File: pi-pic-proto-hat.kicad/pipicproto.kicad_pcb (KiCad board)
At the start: 2 copper layers, 65 x 56 mm, 26 parts, among them J1 RUN/~PGM~, J10 Conn_01x13_Male, J2 Conn_SW1, J22 Conn_01x13_Male, J6 Barrel_Jack_Switch, J7 Conn_01x24_Male, J8 Conn_01x06_Male, J9 Conn_01x02_Male, P1 Conn_02x20_Odd_Even, Q1 IRF4905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

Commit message: moved button to right of power-jack
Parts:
- added ?: , , F.Cu at (244.4, 129.5)
- added ?: , , F.Cu at (244.7, 129.1)
- moved SW1 18.4 mm to (258.5, 129.9), turned to 180 degrees
- moved J2 6.39 mm to (247.2, 130.5), turned to 180 degrees
- moved J9 2.09 mm to (247.3, 124.0)
- moved U1 2.09 mm to (257.2, 124.1)
- moved R5 2.09 mm to (258.9, 117.4)
- moved C1 2.09 mm to (251.7, 126.9)
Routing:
- net Net-(J2-Pad2): track 28.0 -> 32.2 mm, vias 0 -> 1
- net +5VP: track 20.9 -> 25.0 mm
- net /MCLR: track 9.64 -> 6.06 mm
- net GND: track 36.1 -> 39.5 mm
- net /DAT: track 8.27 -> 10.8 mm
- net /CLK: track 19.3 -> 21.1 mm
- net /GPIO16: track 34.9 -> 33.4 mm
- net Net-(R2-Pad2): track 28.3 -> 29.2 mm
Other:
- board text added: "(SW1)"

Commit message: V2.14: removed dead button from power connector
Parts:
- removed ? (x2): , 
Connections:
- J22 pad 7: Net-(J22-Pad7) -> +3V3

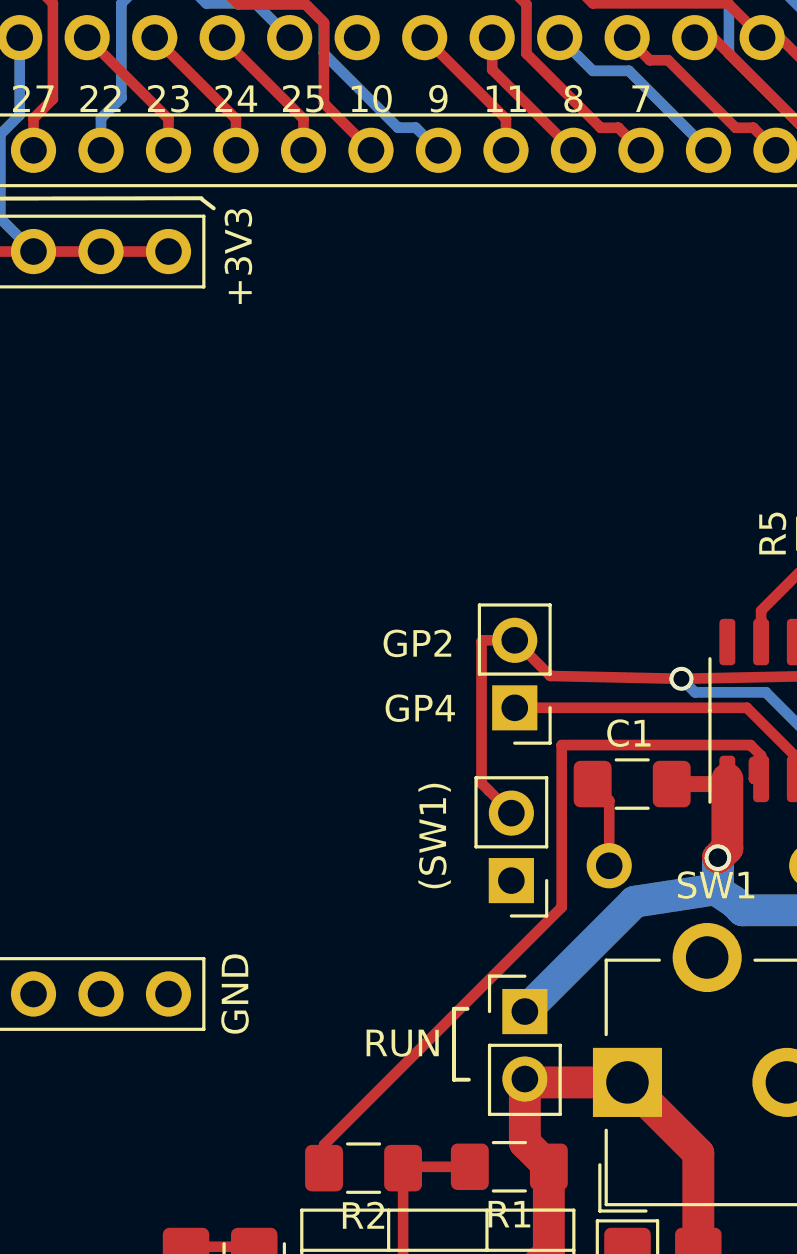
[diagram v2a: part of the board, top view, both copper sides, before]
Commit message: V2.15: added connector for +5P (5V permanently on)
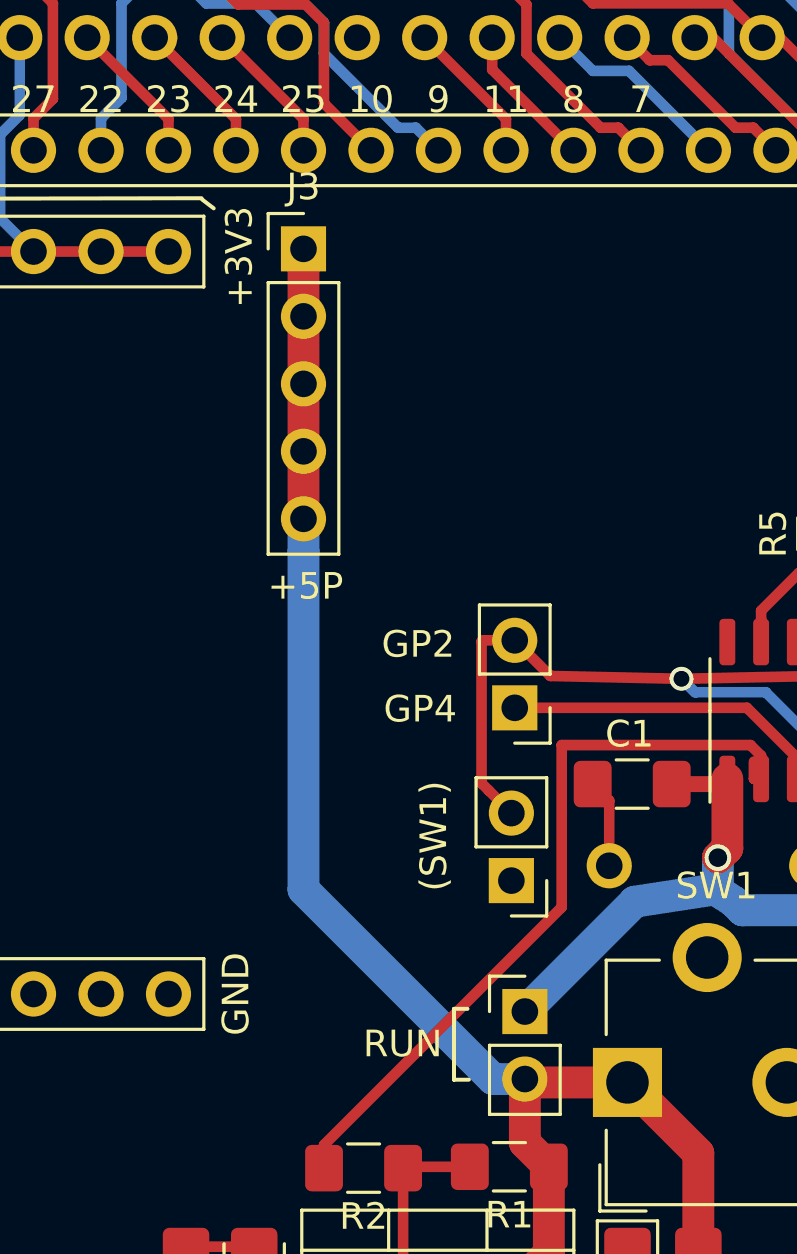
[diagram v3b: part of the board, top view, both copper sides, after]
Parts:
- added J3: Conn_01x05_Male, Connector_PinHeader_2.54mm:PinHeader_1x05_P2.54mm_Vertical, F.Cu at (239.4, 106.7)
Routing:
- net +5P: track 20.5 -> 55.9 mm
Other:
- board text added: "+5P"
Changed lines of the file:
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@@
   (general
     (thickness 1.6)
-    (drawings 68)
-    (tracks 249)
+    (drawings 69)
+    (tracks 257)
     (zones 0)
-    (modules 26)
+    (modules 27)
     (nets 45)
   )
@@
     (add_net +5VP)
   )
+  (module Connector_PinHeader_2.54mm:PinHeader_1x05_P2.54mm_Vertical (layer F.Cu)
+    (at 239.37 106.7184)
+    (descr "Through hole straight pin header, 1x05, 2.54mm pitch, single row")
+    (tags "Through hole pin header THT 1x05 2.54mm single row")
+    (fp_text reference J3 (at 0 -2.33) (layer F.SilkS)
+      (effects (font (size 1 1) (thickness 0.15)))
+    )
+    (fp_text value Conn_01x05_Male (at 0 12.49) (layer F.Fab)
+      (effects (font (size 1 1) (thickness 0.15)))
+    )
+    (fp_text user %R (at 0 5.08 90) (layer F.Fab)
+      (effects (font (size 1 1) (thickness 0.15)))
+    )
+    (fp_line (start 1.8 -1.8) (end -1.8 -1.8) (layer F.CrtYd) (width 0.05))
+    (fp_line (start 1.8 11.95) (end 1.8 -1.8) (layer F.CrtYd) (width 0.05))
+    (fp_line (start -1.8 11.95) (end 1.8 11.95) (layer F.CrtYd) (width 0.05))
+    (fp_line (start -1.8 -1.8) (end -1.8 11.95) (layer F.CrtYd) (width 0.05))
+    (fp_line (start -1.33 -1.33) (end 0 -1.33) (layer F.SilkS) (width 0.12))
+    (fp_line (start -1.33 0) (end -1.33 -1.33) (layer F.SilkS) (width 0.12))
+    (fp_line (start -1.33 1.27) (end 1.33 1.27) (layer F.SilkS) (width 0.12))
+    (fp_line (start 1.33 1.27) (end 1.33 11.49) (layer F.SilkS) (width 0.12))
+    (fp_line (start -1.33 1.27) (end -1.33 11.49) (layer F.SilkS) (width 0.12))
+    (fp_line (start -1.33 11.49) (end 1.33 11.49) (layer F.SilkS) (width 0.12))
+    (fp_line (start -1.27 -0.635) (end -0.635 -1.27) (layer F.Fab) (width 0.1))
+    (fp_line (start -1.27 11.43) (end -1.27 -0.635) (layer F.Fab) (width 0.1))
+    (fp_line (start 1.27 11.43) (end -1.27 11.43) (layer F.Fab) (width 0.1))
+    (fp_line (start 1.27 -1.27) (end 1.27 11.43) (layer F.Fab) (width 0.1))
+    (fp_line (start -0.635 -1.27) (end 1.27 -1.27) (layer F.Fab) (width 0.1))
+    (pad 5 thru_hole oval (at 0 10.16) (size 1.7 1.7) (drill 1) (layers *.Cu *.Mask)
+      (net 41 +5P))
+    (pad 4 thru_hole oval (at 0 7.62) (size 1.7 1.7) (drill 1) (layers *.Cu *.Mask)
+      (net 41 +5P))
+    (pad 3 thru_hole oval (at 0 5.08) (size 1.7 1.7) (drill 1) (layers *.Cu *.Mask)
+      (net 41 +5P))
+    (pad 2 thru_hole oval (at 0 2.54) (size 1.7 1.7) (drill 1) (layers *.Cu *.Mask)
+      (net 41 +5P))
+    (pad 1 thru_hole rect (at 0 0) (size 1.7 1.7) (drill 1) (layers *.Cu *.Mask)
+      (net 41 +5P))
+    (model ${KISYS3DMOD}/Connector_PinHeader_2.54mm.3dshapes/PinHeader_1x05_P2.54mm_Vertical.wrl
+      (at (xyz 0 0 0))
+      (scale (xyz 1 1 1))
+      (rotate (xyz 0 0 0))
+    )
+  )
   (module user:SW_PUSH_SLIM_1x4 (layer F.Cu)
     (at 258.4962 129.934 180)
@@
       (rotate (xyz 0 0 0))
     )
+  )
+  (gr_text +5P (at 239.4462 119.4184) (layer F.SilkS)
+    (effects (font (size 1 1) (thickness 0.15)))
   )
   (gr_text "(SW1)" (at 244.2722 128.8164 90) (layer F.SilkS)
@@
   (segment (start 247.7012 140.3591) (end 248.6045 141.2624) (width 1.2) (layer F.Cu) (net 41) (status 20))
   (segment (start 247.7012 137.9604) (end 247.7012 140.3591) (width 1.2) (layer F.Cu) (net 41) (status 10))
+  (segment (start 239.37 118.080481) (end 239.37 116.8784) (width 1.2) (layer B.Cu) (net 41))
+  (segment (start 239.37 130.831281) (end 239.37 118.080481) (width 1.2) (layer B.Cu) (net 41))
+  (segment (start 246.499119 137.9604) (end 239.37 130.831281) (width 1.2) (layer B.Cu) (net 41))
+  (segment (start 247.7012 137.9604) (end 246.499119 137.9604) (width 1.2) (layer B.Cu) (net 41))
+  (segment (start 239.37 116.8784) (end 239.37 114.3384) (width 1.2) (layer F.Cu) (net 41))
+  (segment (start 239.37 111.7984) (end 239.37 109.2584) (width 1.2) (layer F.Cu) (net 41))
+  (segment (start 239.37 109.2584) (end 239.37 106.7184) (width 1.2) (layer F.Cu) (net 41))
+  (segment (start 239.37 114.3384) (end 239.37 111.7984) (width 1.2) (layer F.Cu) (net 41))
   (segment (start 237.5158 144.2707) (end 234.9504 144.2707) (width 0.4) (layer F.Cu) (net 42) (status 30))
   (segment (start 254.229 147.2457) (end 251.562 147.2457) (width 0.4) (layer F.Cu) (net 43) (status 30))

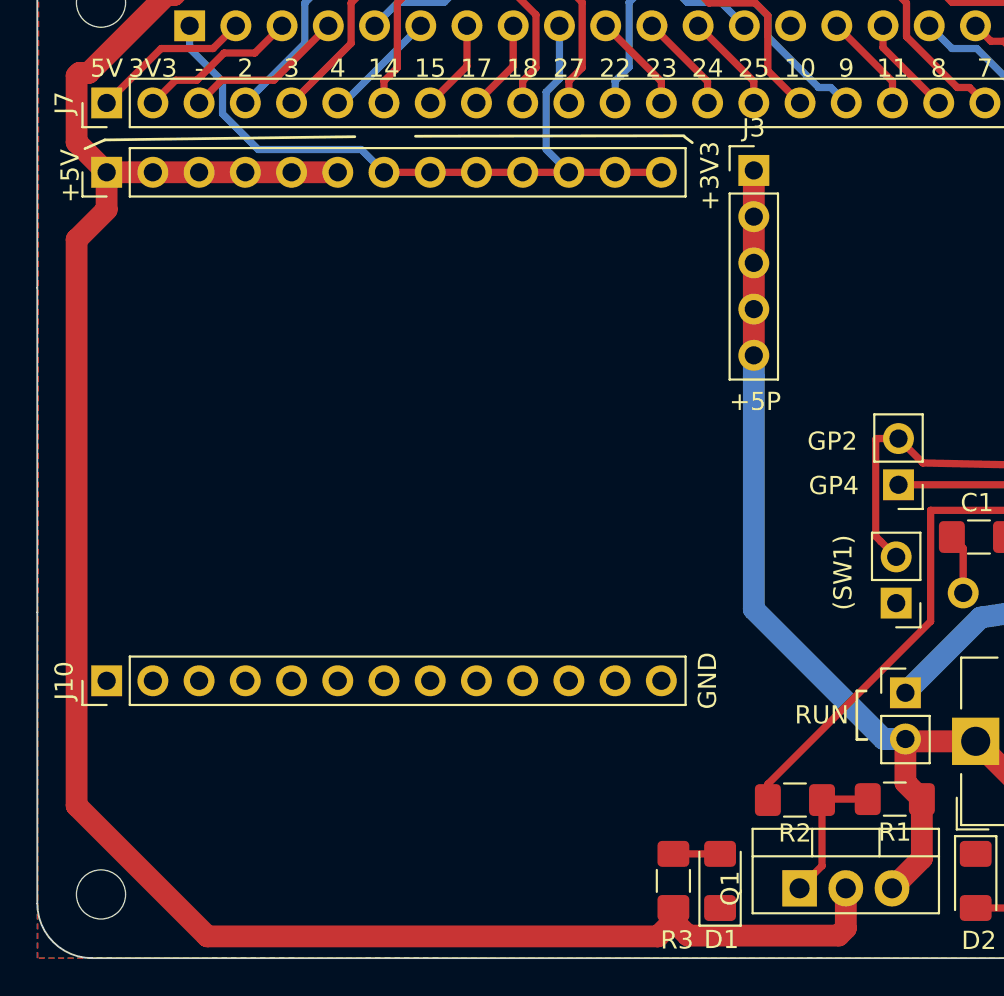
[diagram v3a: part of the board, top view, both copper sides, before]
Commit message: V2.16: added regulator and connector for +3V3P (3V3 permanently on)
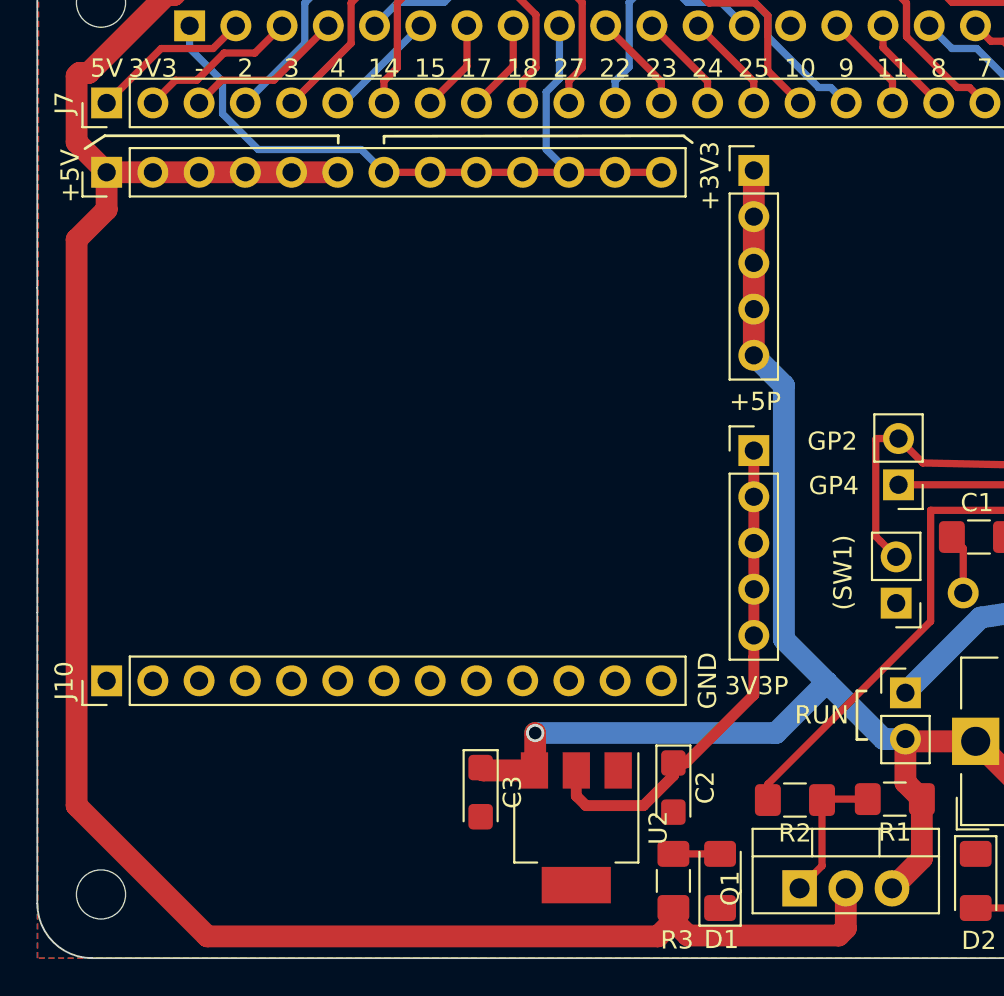
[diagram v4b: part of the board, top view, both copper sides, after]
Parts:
- added C2: 10µF, Capacitor_Tantalum_SMD:CP_EIA-3216-18_Kemet-A, F.Cu at (235.0, 140.6)
- added C3: 10µF, Capacitor_Tantalum_SMD:CP_EIA-3216-18_Kemet-A, F.Cu at (224.4, 140.9)
- added J4: Conn_3V3P, Connector_PinHeader_2.54mm:PinHeader_1x05_P2.54mm_Vertical, F.Cu at (239.4, 122.1)
- added U2: TLV1117-33, Package_TO_SOT_SMD:SOT-223, F.Cu at (229.6, 142.8)
- J3: value Conn_01x05_Male -> Conn_5P
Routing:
- net Net-(C2-Pad1): track 0.00 -> 28.0 mm
- net +5P: track 55.9 -> 78.1 mm, vias 0 -> 1
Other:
- board text added: "3V3P"

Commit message: V2.17: connect switch to GP4 instead of GP2
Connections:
- J9 pad 1: Net-(J9-Pad1) -> Net-(J2-Pad2)
- J9 pad 2: Net-(J2-Pad2) -> Net-(J9-Pad2)
- U1 pad 3: Net-(J9-Pad1) -> Net-(J2-Pad2)
- U1 pad 5: Net-(J2-Pad2) -> Net-(J9-Pad2)
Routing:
- net Net-(J9-Pad2): track 0.00 -> 13.4 mm
- net Net-(J2-Pad2): track 32.2 -> 19.5 mm, vias 1 -> 0
- net Net-(J9-Pad1): track 12.0 -> 0.00 mm

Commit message: added prototyping area
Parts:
- added REF**: Proto_Area_13x09_P2.54mm_Drill1.0mm, Proto_Area:Proto_Area_13x09, F.Cu at (203.8, 110.4)
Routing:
- net +5V: track 114.1 -> 115.9 mm

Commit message: V2.18: add 5VP and 3V3P connectors bottom left
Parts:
- removed REF**: Proto_Area_13x09_P2.54mm_Drill1.0mm, Proto_Area:Proto_Area_13x09
- added J11: Conn_5P_2, Connector_PinHeader_2.54mm:PinHeader_1x02_P2.54mm_Vertical, F.Cu at (221.1, 139.2)
- added J5: Conn_3V3P_2, Connector_PinHeader_2.54mm:PinHeader_1x02_P2.54mm_Vertical, F.Cu at (221.1, 145.7)
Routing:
- net Net-(C2-Pad1): track 28.0 -> 38.4 mm
- net +5P: track 78.1 -> 84.1 mm
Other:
- board text added: "+3V3P"

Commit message: added prototyping area bottom left
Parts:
- added REF**: Proto_Area_13x09_P2.54mm_Drill1.0mm, Proto_Area:Proto_Area_13x09, F.Cu at (203.8, 110.6)
- added REF**: Proto_Area_02x01_P2.54mm_Drill1.0mm, Proto_Area:Proto_Area_02x01, F.Cu at (204.9, 138.5)
- added REF**: Proto_Area_04x01_P2.54mm_Drill1.0mm, Proto_Area:Proto_Area_04x01, F.Cu at (209.9, 146.2)
- added REF**: Proto_Area_05x03_P2.54mm_Drill1.0mm, Proto_Area:Proto_Area_05x03, F.Cu at (207.4, 138.5)
